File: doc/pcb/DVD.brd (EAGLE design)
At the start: 44.1 x 52.1 mm, 32 parts, among them IC1 7805, IC2 74HC14N

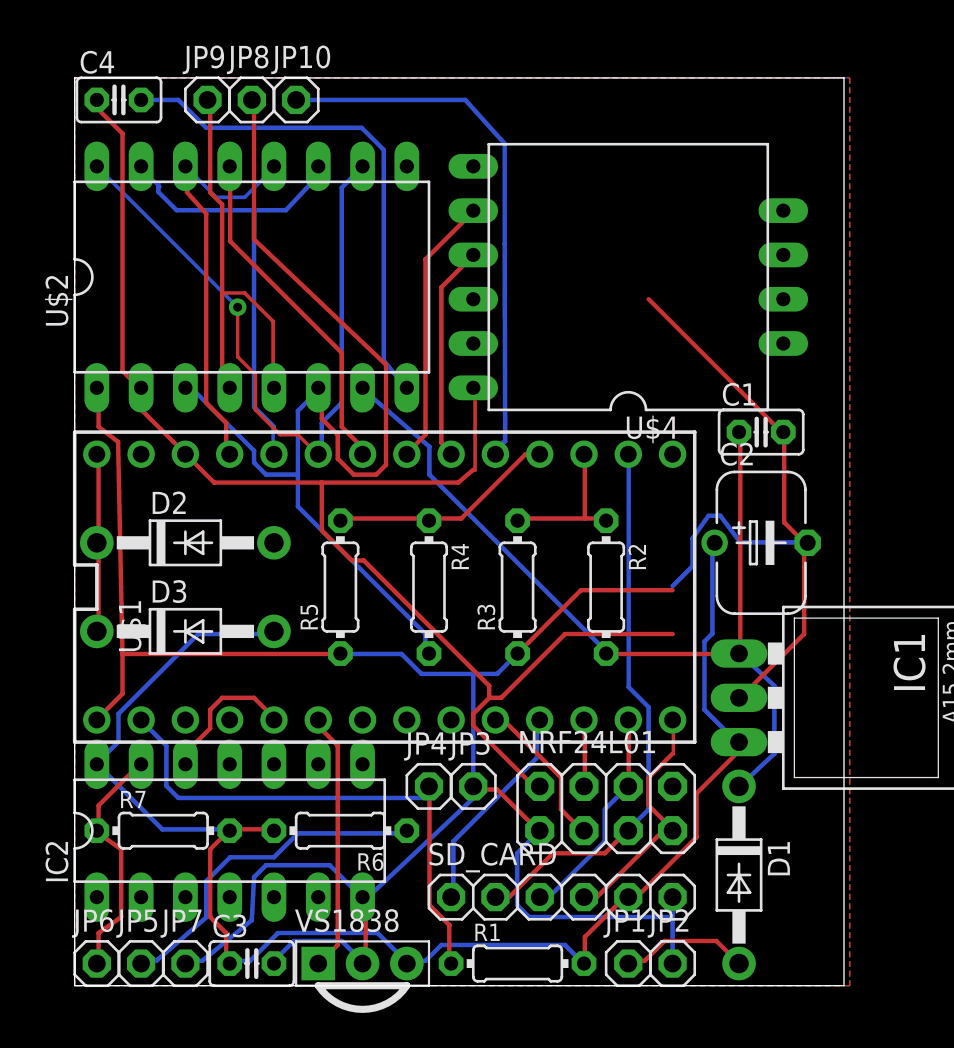
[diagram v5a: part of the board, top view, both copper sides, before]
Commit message: PCB contacted Analog meas with AGND, removed temp meas
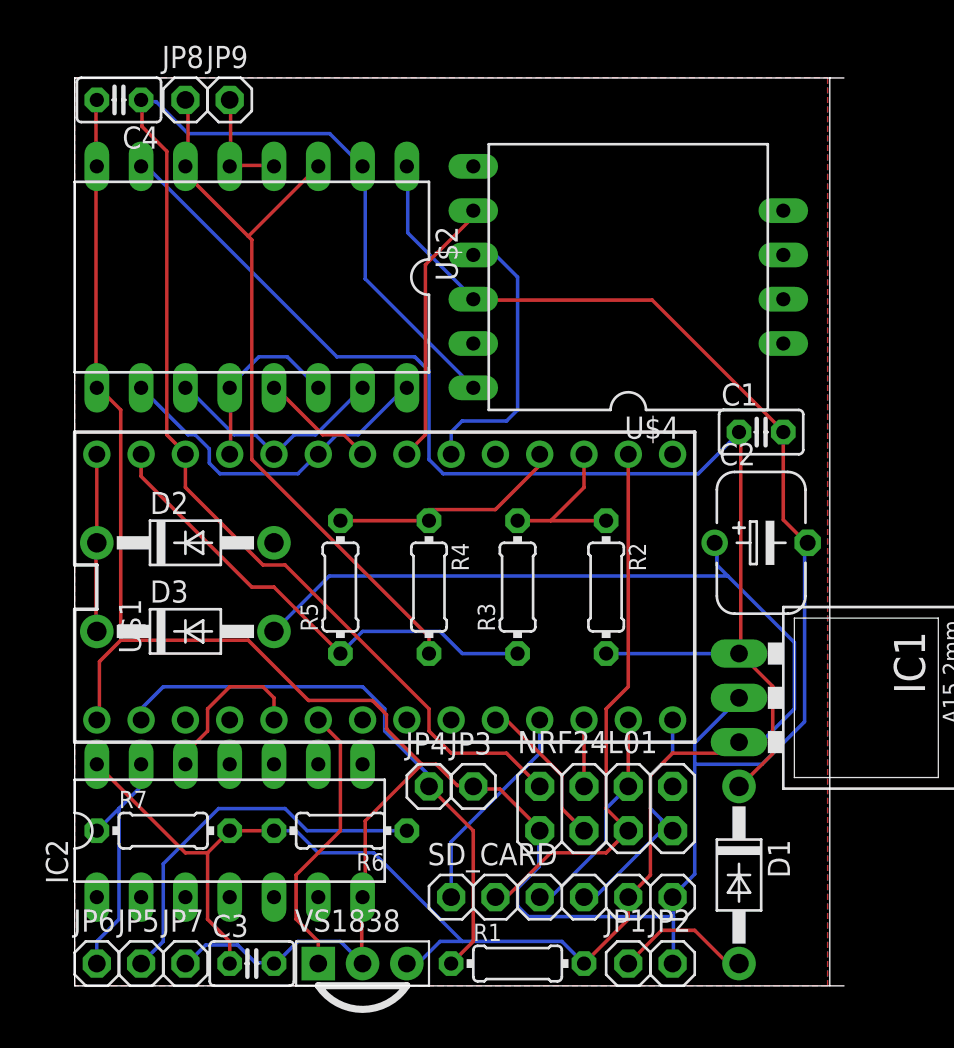
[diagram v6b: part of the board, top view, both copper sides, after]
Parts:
- removed JP10: TEMP, pinhead:1X01
- moved JP8 3.81 mm to (6.35, 68.6)
- moved U$2 2.54 mm to (11.4, 58.4), turned to 180 degrees
- moved JP9 1.27 mm to (8.89, 68.6)
- turned C4 to 180 degrees
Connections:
- removed net JP0: JP10.1, U$1.17/A3
- new net N$6: U$1.17/A3
- net AGND: now also R3.1, R5.1
- net GND: no longer R3.1, R5.1
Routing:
- net JP0: track 31.3 -> 0.00 mm
- net AGND: track 0.00 -> 28.1 mm
- net V+: track 51.1 -> 75.3 mm
- net PWM: track 40.2 -> 19.8 mm, vias 1 -> 0
- net +5V: track 86.8 -> 105.4 mm
- net ENGINE1: track 24.7 -> 6.35 mm
- net JP8: track 60.6 -> 43.6 mm
- net IN2: track 27.7 -> 13.3 mm
- net IN1: track 24.2 -> 10.4 mm
- net STBY: track 19.9 -> 6.67 mm
- net GND: track 186.2 -> 176.5 mm
- net SDA: track 12.6 -> 16.3 mm
- net N$2: track 19.6 -> 22.2 mm
- net N$18: track 30.8 -> 32.9 mm
- net SPEED_SENSOR: track 8.28 -> 9.57 mm
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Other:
- outline, holes or cut-outs redrawn

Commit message: Cleanup of Schematics
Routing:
- net SPEED_SENSOR: track 9.57 -> 8.94 mm
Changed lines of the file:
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@@
 <signal name="+3V3">
 <contactref element="NRF24L01" pad="2"/>
-<contactref element="C4" pad="1"/>
 <contactref element="U$1" pad="3.3V"/>
 <contactref element="U$2" pad="2"/>
@@
 <wire x1="14.6304" y1="66.6496" x2="6.5024" y2="66.6496" width="0.2032" layer="16"/>
 <wire x1="16.51" y1="64.77" x2="14.6304" y2="66.6496" width="0.2032" layer="16"/>
-<wire x1="3.8608" y1="68.4784" x2="3.81" y2="68.58" width="0.2032" layer="16"/>
 <wire x1="3.8608" y1="67.056" x2="3.8608" y2="68.4784" width="0.2032" layer="1"/>
 <wire x1="5.2832" y1="65.6336" x2="3.8608" y2="67.056" width="0.2032" layer="1"/>
 <wire x1="5.2832" y1="49.3776" x2="5.2832" y2="65.6336" width="0.2032" layer="1"/>
 <wire x1="6.2992" y1="48.3616" x2="5.2832" y2="49.3776" width="0.2032" layer="1"/>
-<wire x1="3.8608" y1="68.4784" x2="3.81" y2="68.58" width="0.2032" layer="1"/>
 <wire x1="6.2992" y1="48.3616" x2="6.35" y2="48.26" width="0.2032" layer="1"/>
+<contactref element="C4" pad="1"/>
+<wire x1="3.8608" y1="68.4784" x2="3.81" y2="68.58" width="0" layer="19" extent="16-16"/>
+<wire x1="3.8608" y1="68.4784" x2="3.8608" y2="68.4784" width="0" layer="19" extent="1-16"/>
 </signal>
 <signal name="N$2">
@@
 </signal>
 <signal name="SPEED_SENSOR">
-<contactref element="IC2" pad="12"/>
 <contactref element="U$1" pad="3"/>
-<wire x1="6.35" y1="31.115" x2="6.35" y2="30.48" width="0.2032" layer="1"/>
 <wire x1="7.62" y1="32.385" x2="6.35" y2="31.115" width="0.2032" layer="1"/>
 <wire x1="7.62" y1="33.655" x2="7.62" y2="32.385" width="0.2032" layer="1"/>
@@
 <wire x1="11.43" y1="34.29" x2="10.795" y2="34.925" width="0.2032" layer="1"/>
 <wire x1="11.43" y1="33.02" x2="11.43" y2="34.29" width="0.2032" layer="1"/>
+<contactref element="IC2" pad="12"/>
+<wire x1="6.35" y1="30.48" x2="6.35" y2="31.115" width="0" layer="19" extent="1-1"/>
 </signal>
 <signal name="CSN_SD">

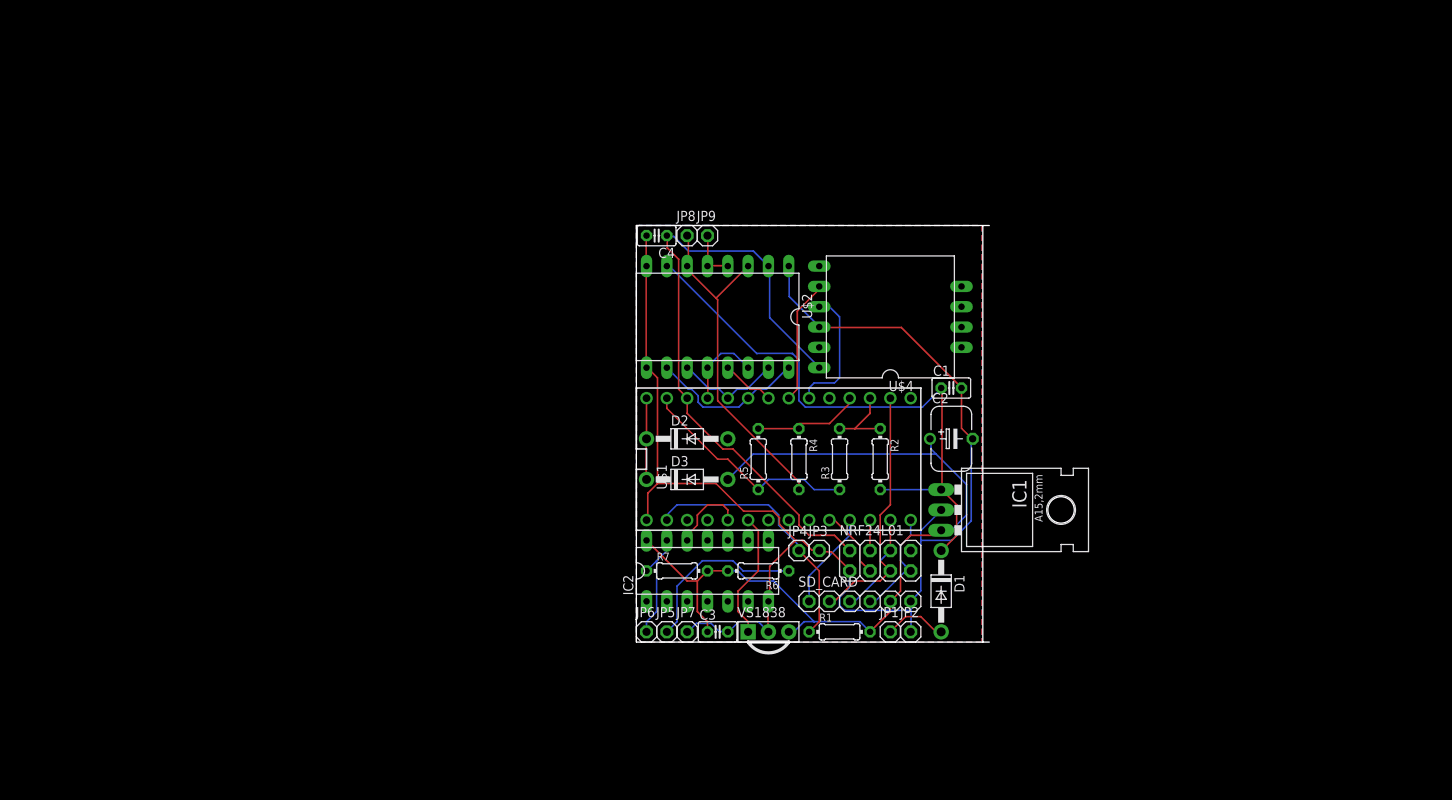
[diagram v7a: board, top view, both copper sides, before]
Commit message: Updated schematic and added groundplate to board of PCB
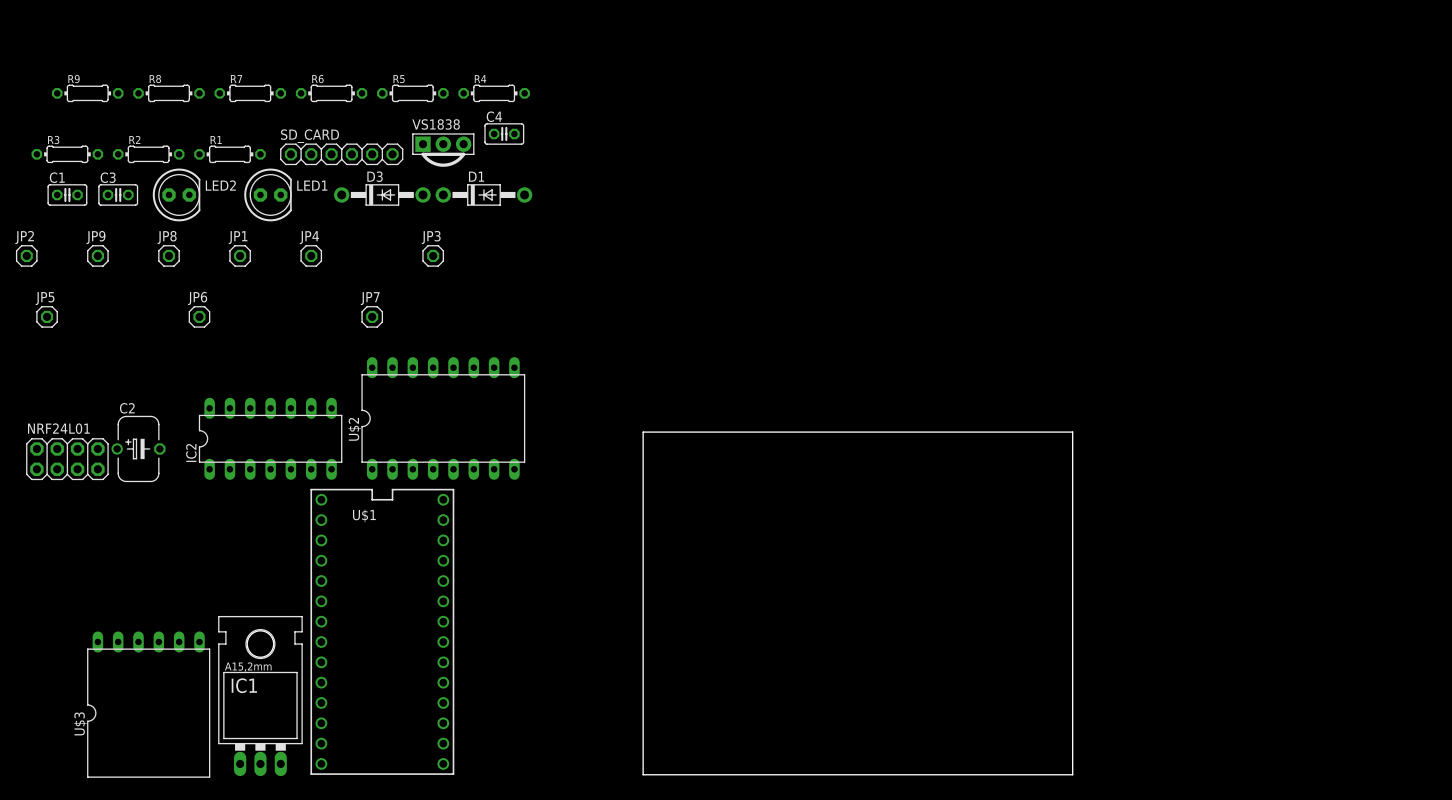
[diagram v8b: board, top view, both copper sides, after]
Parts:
- removed D2: 1N4004, adafruit:DO41-10
- removed U$4: BNO055, DVD:DIL10-6-4
- added LED1, LED2: (no value), adafruit:LED5MM
- added R8, R9: 220, resistor:0204/7
- added U$3: BNO055_LIGHT, DVD:DIL12-6-0
- moved JP2 120.1 mm to (-76.2, 66.0)
- moved C1 113.1 mm to (-71.1, 73.7)
- moved R3 103.8 mm to (-71.1, 78.7), turned to 0 degrees
- moved NRF24L01 102.4 mm to (-71.1, 40.6)
- moved C2 101.6 mm to (-62.2, 41.9)
- moved R2 99.1 mm to (-61.0, 78.7), turned to 0 degrees
- moved R1 96.8 mm to (-50.8, 78.7)
- moved JP1 93.9 mm to (-49.5, 66.0)
- moved IC1 93.2 mm to (-47.0, 6.35), turned to 0 degrees
- moved C3 92.7 mm to (-64.8, 73.7)
- moved JP5 86.9 mm to (-73.7, 58.4)
- moved SD_CARD 85.5 mm to (-36.8, 78.7)
- moved R6 80.1 mm to (-38.1, 86.4), turned to 0 degrees
- moved R7 80.1 mm to (-48.3, 86.4)
- moved JP9 76.2 mm to (-67.3, 66.0)
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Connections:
- removed net N$4: D2.A
- new net N$7: LED1.A, R8.1
- new net N$8: LED2.A, R9.1
- net +3V3: now also U$3.1; no longer U$4.1
- net +5V: now also R8.2
- net 2/3V3OUT: now also U$3.2; no longer U$4.2
- net GND: now also LED1.K, LED2.K, U$3.3; no longer U$4.3
- net N$1: no longer D2.C
- net N$19: now also R9.2
- net SCL: now also U$3.5; no longer U$4.5
- net SDA: now also U$3.4; no longer U$4.4
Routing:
- net GND: track 176.5 -> 0.00 mm
- net +5V: track 105.4 -> 0.00 mm
- net +3V3: track 80.8 -> 0.00 mm
- net V+: track 75.3 -> 0.00 mm
- net JP8: track 43.6 -> 0.00 mm
- net N$18: track 32.9 -> 0.00 mm
- net SCK: track 31.8 -> 0.00 mm
- net AGND: track 28.1 -> 0.00 mm
- net N$2: track 22.2 -> 0.00 mm
- net PWM: track 19.8 -> 0.00 mm
- net SDA: track 16.3 -> 0.00 mm
- net D4_IR: track 16.1 -> 0.00 mm
- net SCL: track 15.6 -> 0.00 mm
- net N$26: track 14.3 -> 0.00 mm
- net MISO: track 14.1 -> 0.00 mm
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- removed copper zone on layer 1, net GND
- removed copper zone on layer 16, net GND
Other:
- board size 44.1 x 52.1 mm -> 53.7 x 42.8 mm
